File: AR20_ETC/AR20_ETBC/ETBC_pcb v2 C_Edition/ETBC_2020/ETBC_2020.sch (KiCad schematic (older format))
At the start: 38 parts, among them IC1 MC33931EK, J1 Conn_02x09_Top_Bottom, J2 Conn_02x05_Odd_Even, Q1 NDS356AP, U1 ACM_2020

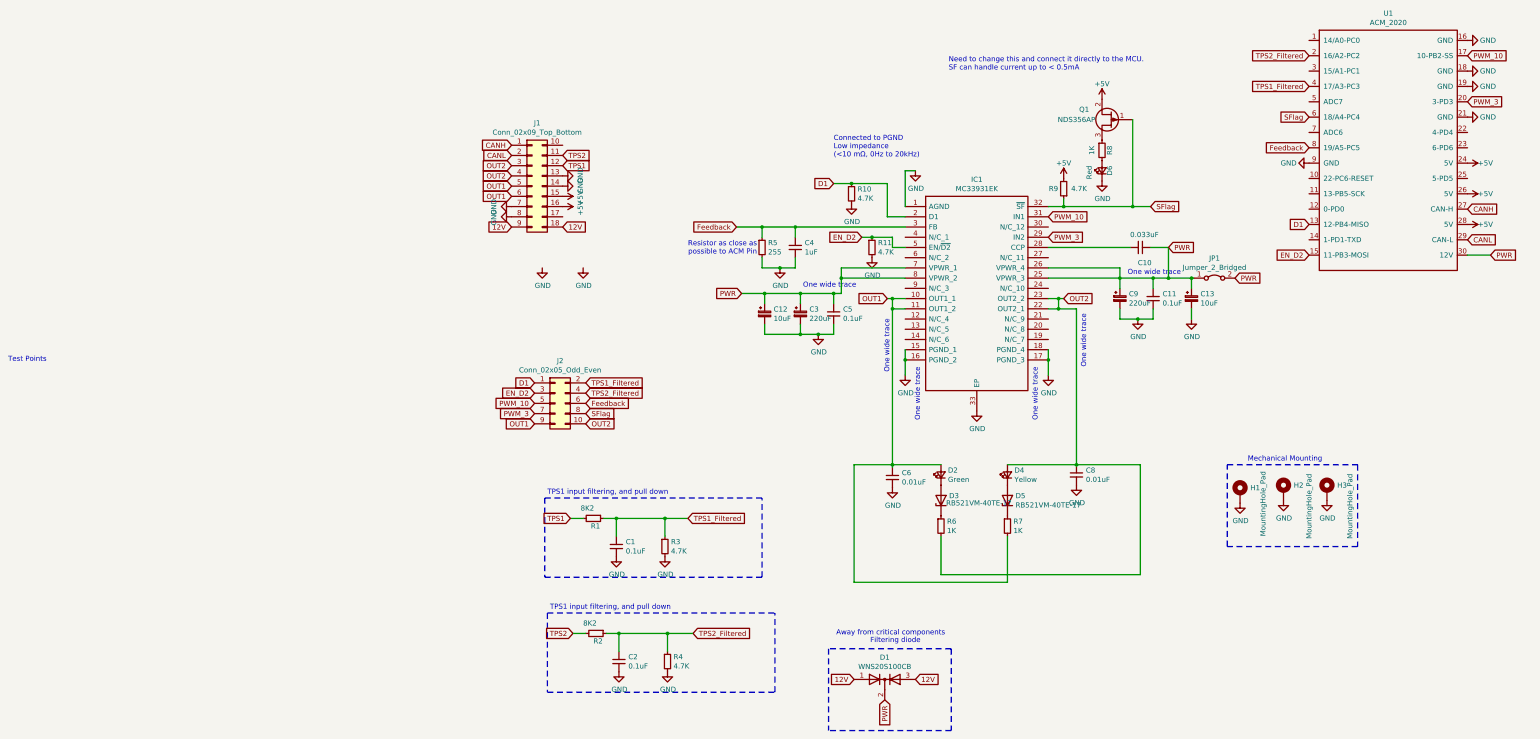
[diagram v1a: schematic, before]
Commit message: V2.3  Better design Done
-New PCB 
-Got rid of superfluous Diode
-Got rid of poor choise Resistors in low pass filter
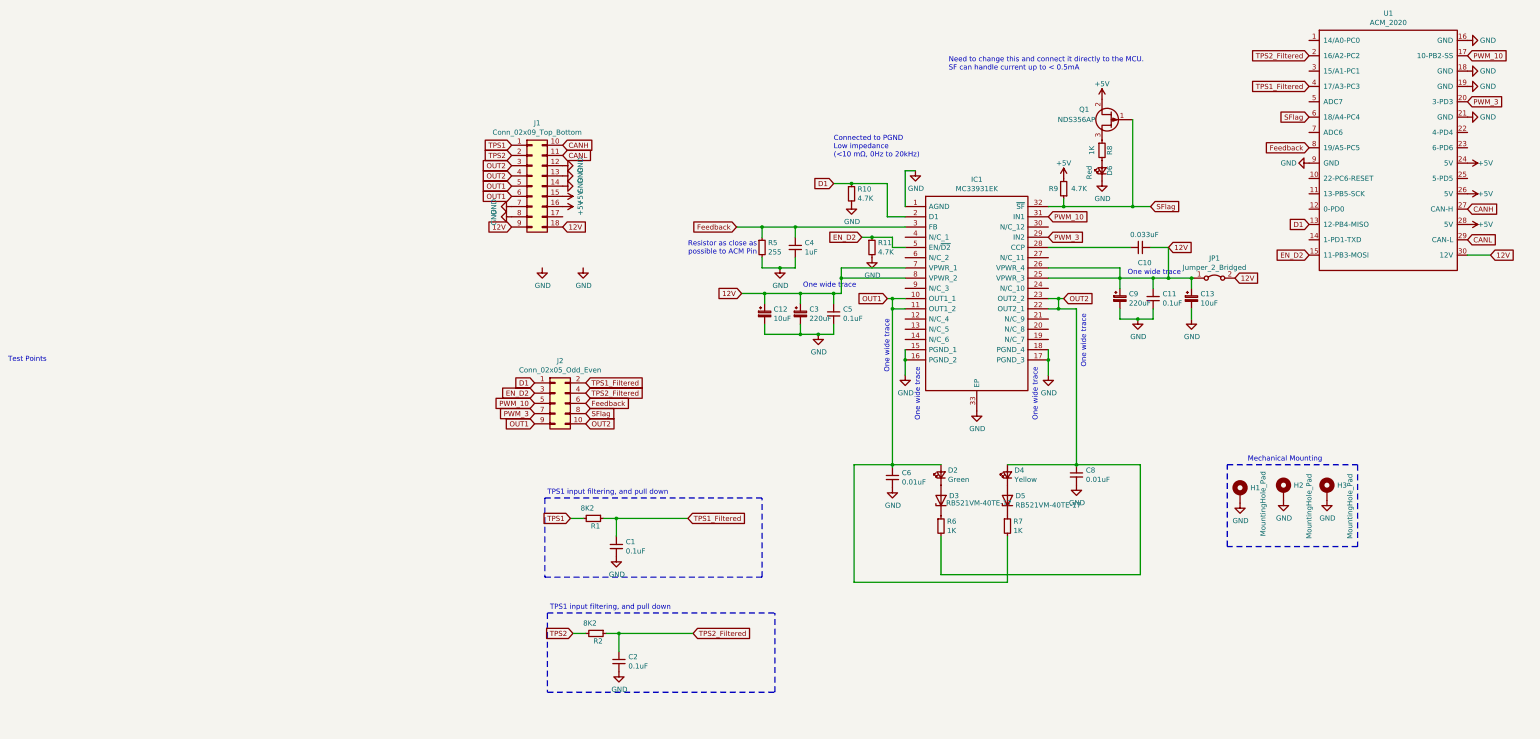
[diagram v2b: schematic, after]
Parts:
- removed D1: WNS20S100CB, Package_TO_SOT_SMD:TO-263-3_TabPin2, symbol Device:D_x2_KCom_AKA
- removed R3, R4: 4.7K, Resistor_SMD:R_0603_1608Metric_Pad1.05x0.95mm_HandSolder, symbol Device:R_Small
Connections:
- net PWR is gone; now on net 12V: C10.1, C11.1, C12.1, C13.1, C3.1, C5.1, C9.1, IC1.25 (VPWR_3), IC1.26 (VPWR_4), IC1.7 (VPWR_1), IC1.8 (VPWR_2), JP1.1 (A), JP1.2 (B), U1.30 (12V)
- net CANH: now also J1.10 (Pin_10); no longer J1.1 (Pin_1)
- net CANL: now also J1.11 (Pin_11); no longer J1.2 (Pin_2)
- net GND: now also J1.12 (Pin_12)
- net TPS1: now also J1.1 (Pin_1); no longer J1.12 (Pin_12)
- net TPS2: now also J1.2 (Pin_2); no longer J1.11 (Pin_11)
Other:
- note removed: "Away from critical components"
- note removed: "Filtering diode"
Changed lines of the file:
@@
 Text GLabel 4650 2775 0    50   Input ~ 0
 EN_D2
-Text GLabel 8300 3175 2    50   Input ~ 0
-PWR
 Connection ~ 7500 3175
 $Comp
@@
 Text GLabel 6475 2775 2    50   Input ~ 0
 PWM_3
-Text GLabel 10800 2950 2    50   Input ~ 0
-PWR
 Wire Wire Line
 	10575 2950 10800 2950
@@
 	1    0    0    -1
 $EndComp
-$Comp
-L Device:R_Small R4
-U 1 1 5E38FCFD
-P 2750 6925
-F 0 "R4" H 2809 6971 50  0000 L CNN
-F 1 "4.7K" H 2809 6880 50  0000 L CNN
-F 2 "Resistor_SMD:R_0603_1608Metric_Pad1.05x0.95mm_HandSolder" H 2750 6925 50  0001 C CNN
-F 3 "~" H 2750 6925 50  0001 C CNN
-F 4 "AR20_ETC_010" H 2750 6925 50  0001 C CNN "AR-ID"
-	1    2750 6925
-	1    0    0    -1
-$EndComp
 Wire Notes Line
 	3675 6100 3675 5325
@@
 Wire Wire Line
 	2275 6650 2275 6825
-Wire Wire Line
-	2275 6650 2750 6650
-Wire Wire Line
-	2750 6650 2750 6825
 Connection ~ 2275 6650
-$Comp
-L power:GND #PWR0120
-U 1 1 5E39A7AF
-P 2750 7025
-F 0 "#PWR0120" H 2750 6775 50  0001 C CNN
-F 1 "GND" H 2755 6852 50  0000 C CNN
-F 2 "" H 2750 7025 50  0001 C CNN
-F 3 "" H 2750 7025 50  0001 C CNN
-	1    2750 7025
-	1    0    0    -1
-$EndComp
 $Comp
 L power:GND #PWR0121
@@
 	1    0    0    -1
 $EndComp
-$Comp
-L Device:R_Small R3
-U 1 1 5E3A3534
-P 2725 5800
-F 0 "R3" H 2784 5846 50  0000 L CNN
-F 1 "4.7K" H 2784 5755 50  0000 L CNN
-F 2 "Resistor_SMD:R_0603_1608Metric_Pad1.05x0.95mm_HandSolder" H 2725 5800 50  0001 C CNN
-F 3 "~" H 2725 5800 50  0001 C CNN
-F 4 "AR20_ETC_010" H 2725 5800 50  0001 C CNN "AR-ID"
-	1    2725 5800
-	1    0    0    -1
-$EndComp
 Wire Wire Line
 	1800 5525 1925 5525
@@
 Wire Wire Line
 	2250 5525 2250 5700
-Wire Wire Line
-	2250 5525 2725 5525
-Wire Wire Line
-	2725 5525 2725 5700
 Connection ~ 2250 5525
-$Comp
-L power:GND #PWR0122
-U 1 1 5E3A3540
-P 2725 5900
-F 0 "#PWR0122" H 2725 5650 50  0001 C CNN
-F 1 "GND" H 2730 5727 50  0000 C CNN
-F 2 "" H 2725 5900 50  0001 C CNN
-F 3 "" H 2725 5900 50  0001 C CNN
-	1    2725 5900
-	1    0    0    -1
-$EndComp
 $Comp
 L power:GND #PWR0123
@@
 	1    0    0    -1
 $EndComp
-Wire Wire Line
-	2950 5525 2725 5525
-Connection ~ 2725 5525
-Wire Wire Line
-	3000 6650 2750 6650
-Connection ~ 2750 6650
 Text GLabel 1225 2275 0    50   Input ~ 0
 OUT1
@@
 	1    0    0    -1
 $EndComp
-Text GLabel 1725 2075 2    50   Input ~ 0
+Text GLabel 1225 1875 0    50   Input ~ 0
 TPS1
-Text GLabel 1725 1975 2    50   Input ~ 0
+Text GLabel 1225 1975 0    50   Input ~ 0
 TPS2
 $Comp
@@
 Text GLabel 10575 2800 2    50   Input ~ 0
 CANL
-Text GLabel 1225 1975 0    50   Input ~ 0
+Text GLabel 1725 1975 2    50   Input ~ 0
 CANL
 $Comp
@@
 Text Notes 4925 4100 1    50   ~ 0
 One wide trace
-Text GLabel 1225 1875 0    50   Input ~ 0
+Text GLabel 1725 1875 2    50   Input ~ 0
 CANH
 $Comp
@@
 Text Notes -3700 4000 0    50   ~ 0
 Test Points
-Text GLabel 3475 3325 0    50   Input ~ 0
-PWR
 $Comp
 L Jumper:Jumper_2_Bridged JP1
@@
 Wire Wire Line
 	7650 3175 7875 3175
-Text GLabel 7650 2875 2    50   Input ~ 0
-PWR
 $Comp
 L power:GND #PWR0134
@@
 	1    0    0    -1
 $EndComp
-Wire Notes Line
-	5525 6800 5525 7600
-Wire Notes Line
-	4325 6800 4325 7600
-Wire Notes Line
-	5525 7600 4325 7600
-Text GLabel 5175 7100 2    50   Input ~ 0
+Text GLabel 8300 3175 2    50   Input ~ 0
 12V
-Text GLabel 4575 7100 0    50   Input ~ 0
+Text GLabel 3475 3325 0    50   Input ~ 0
 12V
-$Comp
-L Device:D_x2_KCom_AKA D1
-U 1 1 5E63A4C5
-P 4875 7100
-F 0 "D1" H 4875 7316 50  0000 C CNN
-F 1 "WNS20S100CB" H 4875 7225 50  0000 C CNN
-F 2 "Package_TO_SOT_SMD:TO-263-3_TabPin2" H 4875 7100 50  0001 C CNN
-F 3 "~" H 4875 7100 50  0001 C CNN
-	1    4875 7100
-	1    0    0    -1
-$EndComp
-Text Notes 4400 6675 0    50   ~ 0
-Away from critical components
-Wire Notes Line
-	5525 6800 4325 6800
-Text GLabel 4875 7300 3    50   Input ~ 0
-PWR
-Text Notes 5225 6750 2    50   ~ 0
-Filtering diode
+Text GLabel 7650 2875 2    50   Input ~ 0
+12V
+Wire Wire Line
+	2250 5525 2950 5525
+Wire Wire Line
+	2275 6650 3000 6650
+Text GLabel 10800 2950 2    50   Input ~ 0
+12V
+$Comp
+L power:GND #PWR?
+U 1 1 5F9B44FA
+P 1725 2075
+F 0 "#PWR?" H 1725 1825 50  0001 C CNN
+F 1 "GND" H 1730 1902 50  0000 C CNN
+F 2 "" H 1725 2075 50  0001 C CNN
+F 3 "" H 1725 2075 50  0001 C CNN
+	1    1725 2075
+	0    -1   -1   0
+$EndComp
 $EndSCHEMATC

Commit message: slight schematics cleanup
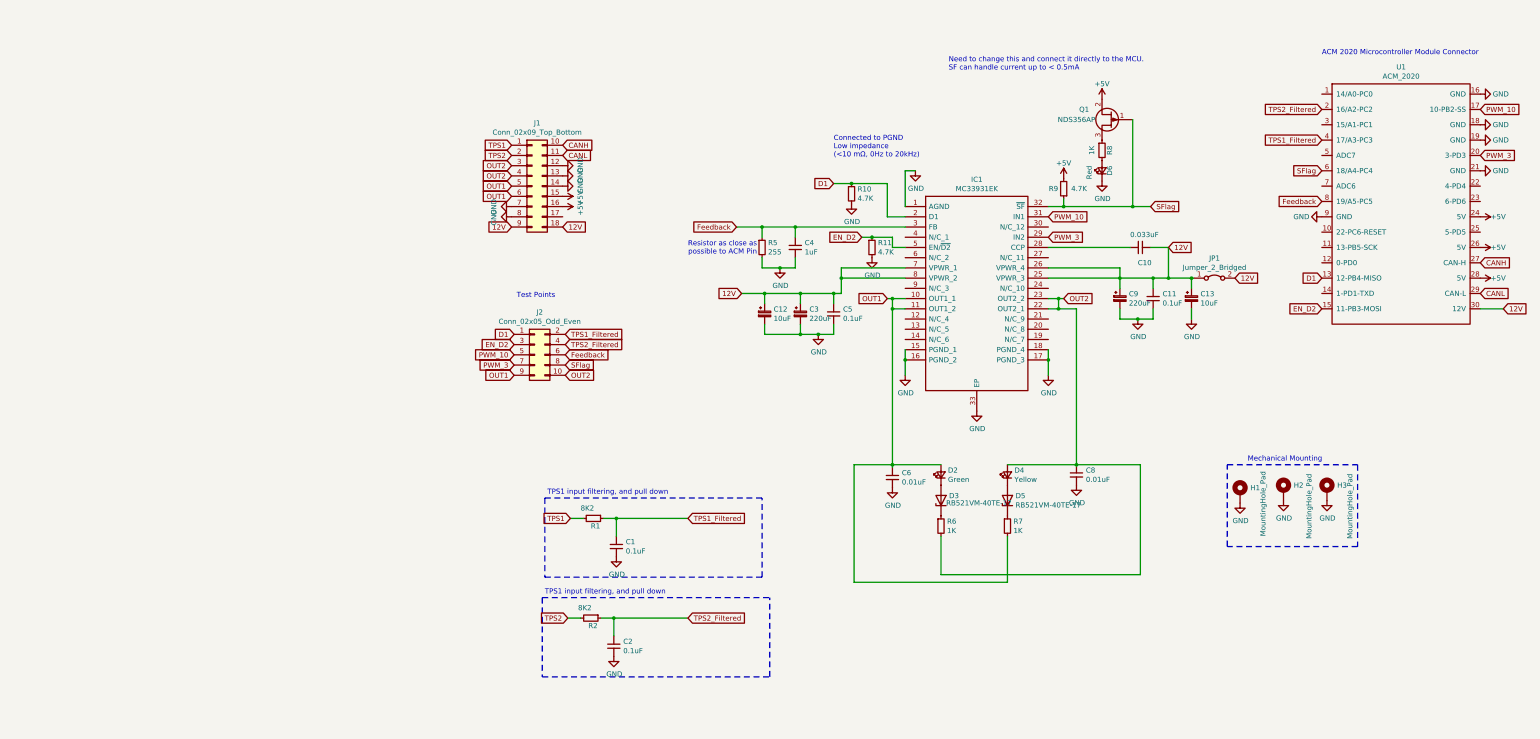
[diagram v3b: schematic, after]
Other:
- note added: "ACM 2020 Microcontroller Module Connector"
- note removed: "One wide trace"
- moved on the sheet: C2, J2, R2, U1
